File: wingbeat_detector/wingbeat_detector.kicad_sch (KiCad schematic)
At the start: 0 parts

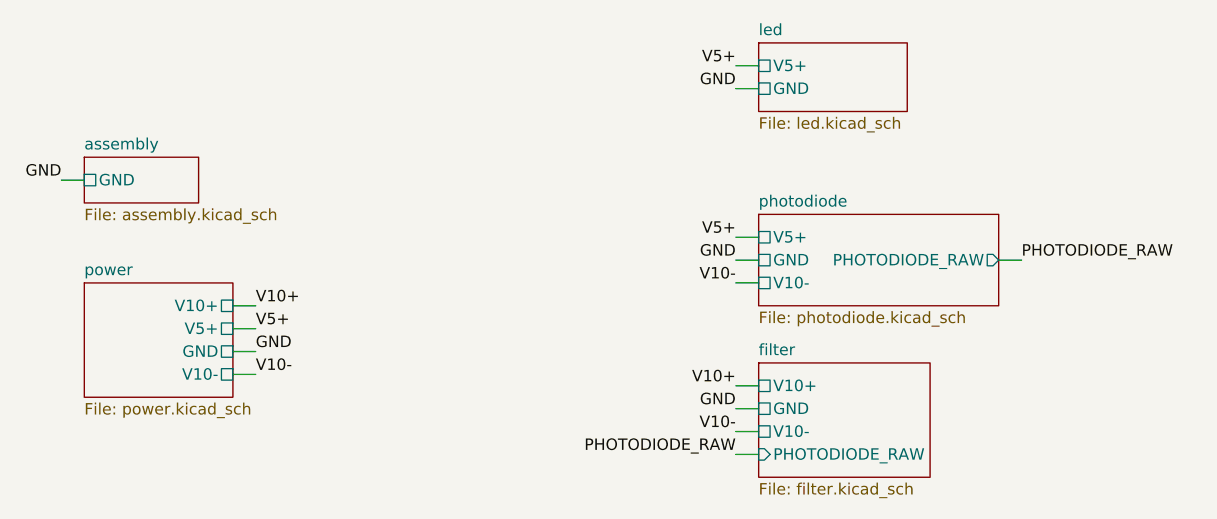
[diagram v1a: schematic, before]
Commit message: Remove LED
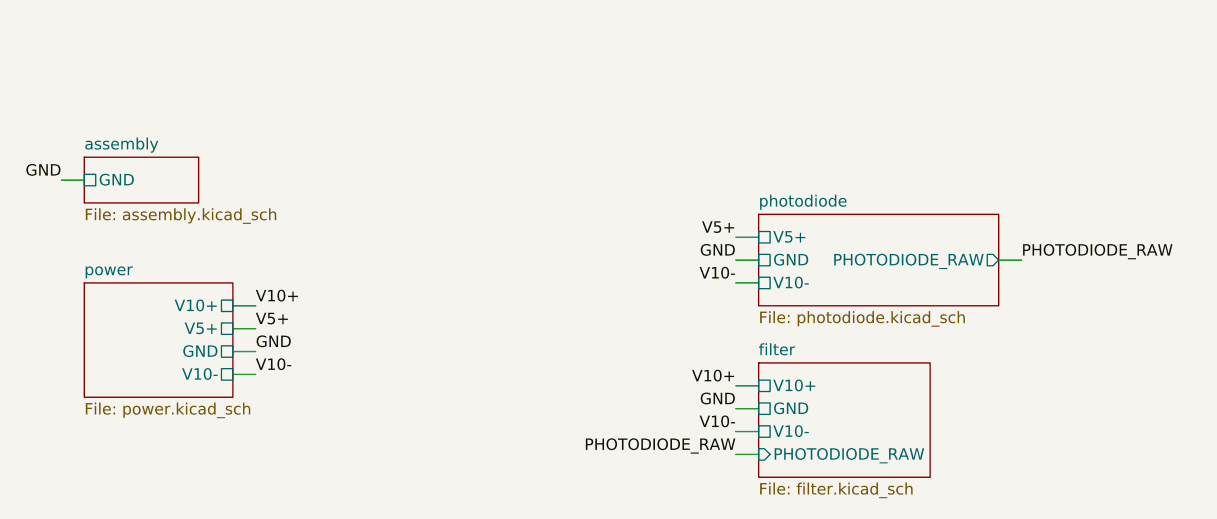
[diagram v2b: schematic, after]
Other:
- removed sheet led
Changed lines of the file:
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@@
   (title_block
     (title "wingbeat_detector")
-    (date "2023-03-31")
-    (rev "3.2")
+    (date "2023-10-05")
+    (rev "4.0")
     (company "Peter Polidoro")
   )
-  (wire (pts (xy 166.37 77.47) (xy 168.91 77.47))
-    (stroke (width 0) (type default))
-  )
   (wire (pts (xy 166.37 101.6) (xy 168.91 101.6))
-    (stroke (width 0) (type default))
-  )
-  (wire (pts (xy 166.37 80.01) (xy 168.91 80.01))
     (stroke (width 0) (type default))
   )
@@
     (effects (font (size 1.27 1.27)) (justify right bottom))
   )
-  (label "GND" (at 166.37 80.01 180) (fields_autoplaced)
-    (effects (font (size 1.27 1.27)) (justify right bottom))
-  )
   (label "GND" (at 166.37 99.06 180) (fields_autoplaced)
     (effects (font (size 1.27 1.27)) (justify right bottom))
@@
   (label "V5+" (at 113.03 106.68 0) (fields_autoplaced)
     (effects (font (size 1.27 1.27)) (justify left bottom))
-  )
-  (label "V5+" (at 166.37 77.47 180) (fields_autoplaced)
-    (effects (font (size 1.27 1.27)) (justify right bottom))
   )
   (label "PHOTODIODE_RAW" (at 198.12 99.06 0) (fields_autoplaced)
@@
       )
     )
-  )
-  (sheet (at 168.91 74.93) (size 16.51 7.62) (fields_autoplaced)
-    (stroke (width 0.1524) (type solid))
-    (fill (color 0 0 0 0.0000))
-    (property "Sheetname" "led" (at 168.91 74.2184 0)
-      (effects (font (size 1.27 1.27)) (justify left bottom))
-    )
-    (property "Sheetfile" "led.kicad_sch" (at 168.91 83.1346 0)
-      (effects (font (size 1.27 1.27)) (justify left top))
-    )
-    (pin "GND" passive (at 168.91 80.01 180)
-      (effects (font (size 1.27 1.27)) (justify left))
-    )
-    (pin "V5+" passive (at 168.91 77.47 180)
-      (effects (font (size 1.27 1.27)) (justify left))
-    )
-    (instances
-      (project "wingbeat_detector"
-        (path "/cc457ebc-4af6-4663-b19f-8cb38f061cb4" (page "5"))
-      )
-    )

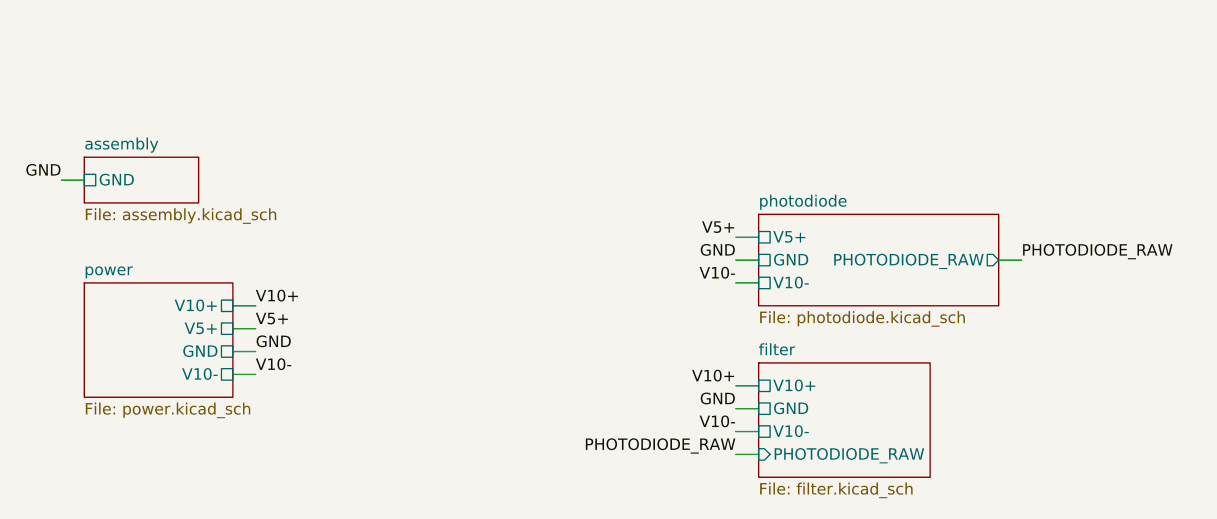
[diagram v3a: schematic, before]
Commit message: First attempt at routing
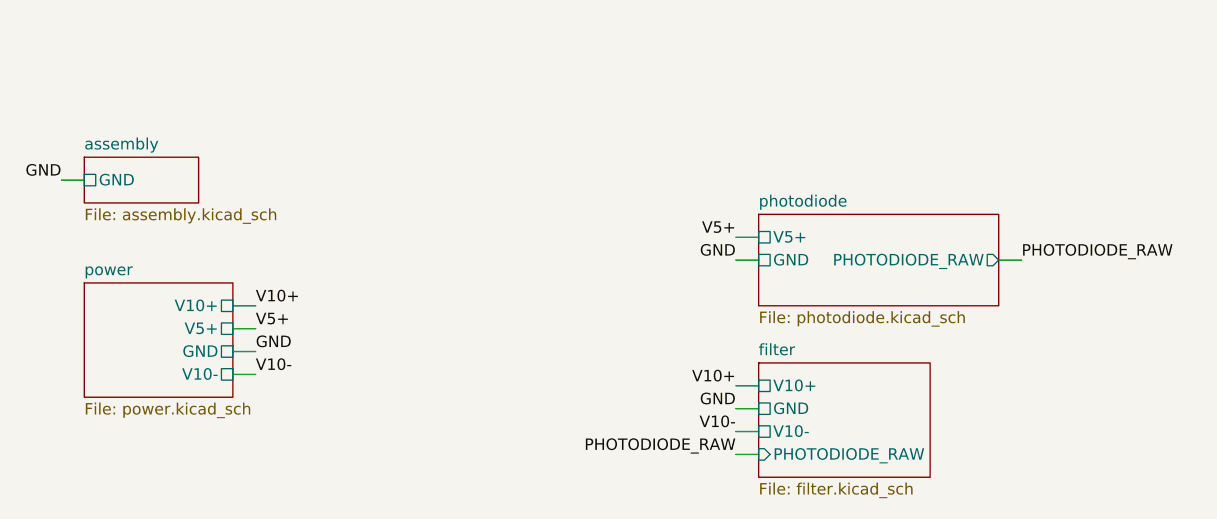
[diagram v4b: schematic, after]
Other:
- sheet photodiode ports: added none; removed V10-
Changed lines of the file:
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@@
   (title_block
     (title "wingbeat_detector")
-    (date "2023-12-08")
+    (date "2023-12-11")
     (rev "4.0")
     (company "Peter Polidoro")
-  )
-  (wire (pts (xy 166.37 101.6) (xy 168.91 101.6))
-    (stroke (width 0) (type default))
   )
   (wire (pts (xy 113.03 111.76) (xy 110.49 111.76))
@@
   )
   (label "GND" (at 91.44 90.17 180) (fields_autoplaced)
-    (effects (font (size 1.27 1.27)) (justify right bottom))
-  )
-  (label "V10-" (at 166.37 101.6 180) (fields_autoplaced)
     (effects (font (size 1.27 1.27)) (justify right bottom))
   )
@@
       (effects (font (size 1.27 1.27)) (justify right))
     )
-    (pin "V10-" passive (at 168.91 101.6 180)
-      (effects (font (size 1.27 1.27)) (justify left))
-    )
     (instances

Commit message: Adjust tracks and zones
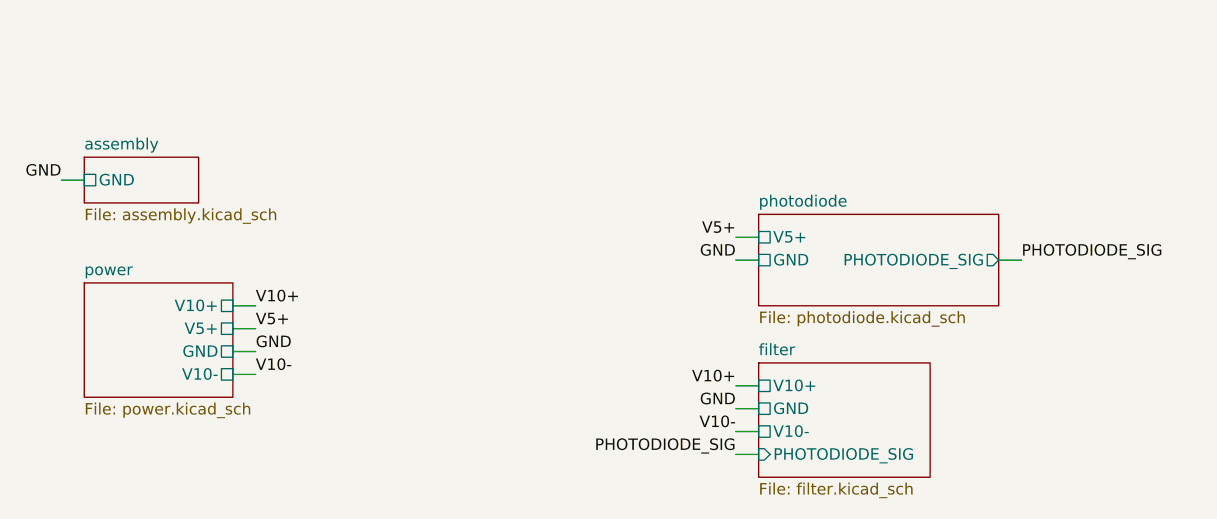
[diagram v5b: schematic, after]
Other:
- sheet filter ports: added PHOTODIODE_SIG; removed PHOTODIODE_RAW
- sheet photodiode ports: added PHOTODIODE_SIG; removed PHOTODIODE_RAW
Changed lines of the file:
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@@
   (title_block
     (title "wingbeat_detector")
-    (date "2023-12-11")
+    (date "2023-12-12")
     (rev "4.0")
     (company "Peter Polidoro")
@@
     (effects (font (size 1.27 1.27)) (justify left bottom))
   )
-  (label "PHOTODIODE_RAW" (at 198.12 99.06 0) (fields_autoplaced)
+  (label "PHOTODIODE_SIG" (at 198.12 99.06 0) (fields_autoplaced)
     (effects (font (size 1.27 1.27)) (justify left bottom))
   )
@@
     (effects (font (size 1.27 1.27)) (justify right bottom))
   )
-  (label "PHOTODIODE_RAW" (at 166.37 120.65 180) (fields_autoplaced)
+  (label "PHOTODIODE_SIG" (at 166.37 120.65 180) (fields_autoplaced)
     (effects (font (size 1.27 1.27)) (justify right bottom))
   )
@@
       (effects (font (size 1.27 1.27)) (justify left))
     )
-    (pin "PHOTODIODE_RAW" input (at 168.91 120.65 180)
+    (pin "PHOTODIODE_SIG" input (at 168.91 120.65 180)
       (effects (font (size 1.27 1.27)) (justify left))
     )
@@
       (effects (font (size 1.27 1.27)) (justify left))
     )
-    (pin "PHOTODIODE_RAW" output (at 195.58 99.06 0)
+    (pin "PHOTODIODE_SIG" output (at 195.58 99.06 0)
       (effects (font (size 1.27 1.27)) (justify right))
     )
